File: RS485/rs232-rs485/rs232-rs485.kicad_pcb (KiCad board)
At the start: 2 copper layers, 10.9 x 10.9 mm, 8 parts, among them J1 Conn_02x04_Counter_Clockwise, J2 Conn_01x03, U1 PIC10F322, U2 MAX3072E

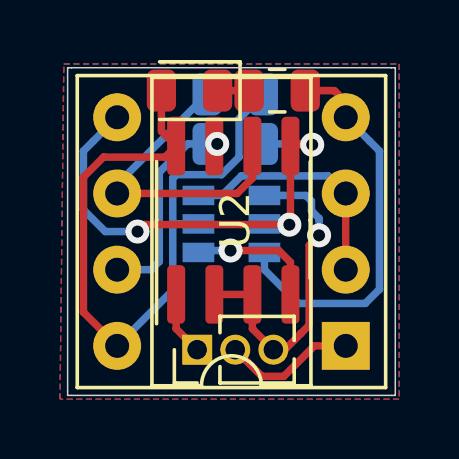
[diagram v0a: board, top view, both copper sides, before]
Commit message: use 2.00mm pin header
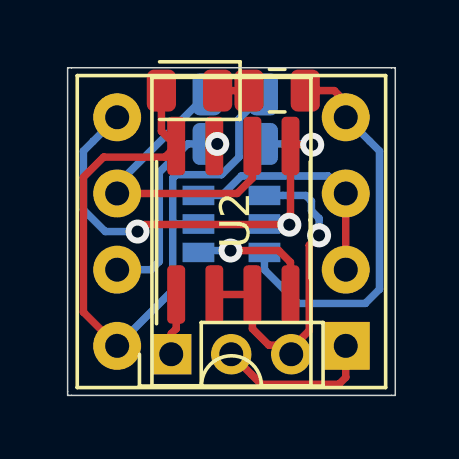
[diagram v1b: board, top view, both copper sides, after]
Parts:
- J2: footprint Connector_PinHeader_1.27mm:PinHeader_1x03_P1.27mm_Vertical -> Connector_PinHeader_2.00mm:PinHeader_1x03_P2.00mm_Vertical
- moved J2 0.88 mm to (128.9, 107.5)
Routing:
- net /RxD: track 4.47 -> 5.38 mm
- removed copper zone on B.Cu, net (none)
- removed copper zone on F.Cu, net (none)
